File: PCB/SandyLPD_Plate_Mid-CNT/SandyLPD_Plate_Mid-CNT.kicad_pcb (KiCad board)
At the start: 2 copper layers, 49.4 x 61 mm, 10 parts

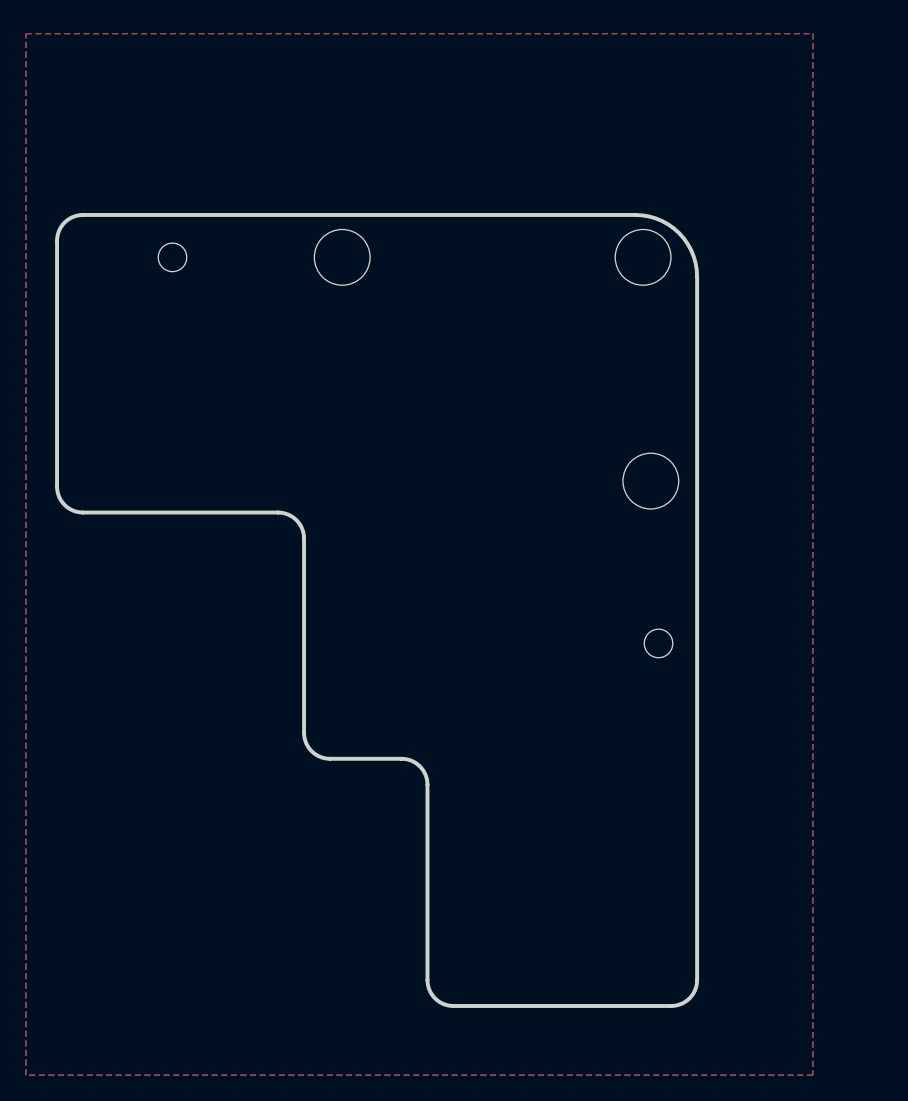
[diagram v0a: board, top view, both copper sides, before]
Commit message: WIP Top基板裏側のソケットを逃す穴を作成中。
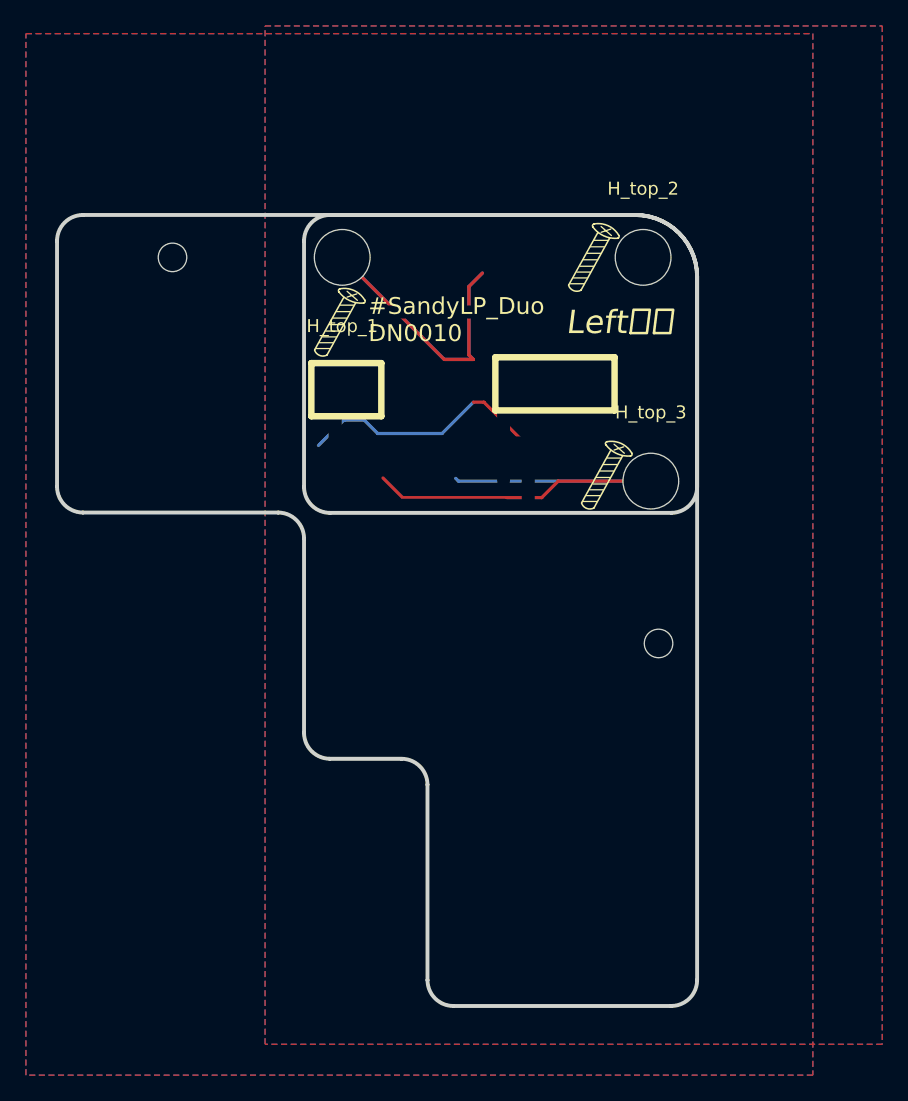
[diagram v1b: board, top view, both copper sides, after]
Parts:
- added REF**: ICON_Screw_Long_Medium, locallib:ICON_Screw_Long_Medium, F.Cu at (149.2, 59.3)
- added REF**: ICON_Screw_Long_Medium, locallib:ICON_Screw_Long_Medium, F.Cu at (148.2, 42.5)
- added REF**: ICON_Screw_Long_Medium, locallib:ICON_Screw_Long_Medium, F.Cu at (128.6, 47.5)
- added REF**: 60_Outline, locallib:SandyLPD_outline_Top, F.Cu at (163.9, 59.2)
- added REF**: ICON_Screw_Long_Medium, locallib:ICON_Screw_Long_Medium, B.Cu at (132.1, 47.1)
- added REF**: ICON_Screw_Long_Medium, locallib:ICON_Screw_Long_Medium, B.Cu at (150.1, 42.9)
- added REF**: ICON_Screw_Long_Medium, locallib:ICON_Screw_Long_Medium, B.Cu at (150.1, 59.3)
- SW_MACRO_L2: footprint locallib:MX-Switch-Hole-with-narrow-frame -> locallib:MX-Switch-Hole-with-narrow-frame-for-socket-escape
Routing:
- net (no net): track 0.00 -> 97.9 mm
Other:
- board text added: "#SandyLP_Duo DN0010"
- board text added: "Left 左"
- board text added: "Right 右"
- board text added: "Top基板うら側のソケットを逃すようにを調整。"
- board text removed: "スペーサー逃し穴のサイズを調整。 コートヤードも調整。"
